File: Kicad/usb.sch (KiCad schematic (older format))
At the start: 1 part

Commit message: Completed Audio sheet.
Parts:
- gave numbers to parts that had none: 1
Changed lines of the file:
@@
 Sheet 5 9
 Title ""
-Date ""
+Date "2020-12-20"
 Rev ""
-Comp ""
-Comment1 ""
-Comment2 ""
+Comp "https://neotron-compute.github.io/"
+Comment1 "Licenced as CC BY-SA"
+Comment2 "Copyright (c) The Neotron Developers, 2020"
 Comment3 ""
 Comment4 ""
@@
 P 1700 1800
 AR Path="/5FDEB111" Ref="J?"  Part="1"
-AR Path="/5FDE7004/5FDEB111" Ref="J?"  Part="1"
-F 0 "J?" H 1757 2267 50  0000 C CNN
+AR Path="/5FDE7004/5FDEB111" Ref="J501"  Part="1"
+F 0 "J501" H 1757 2267 50  0000 C CNN
 F 1 "USB_A" H 1757 2176 50  0000 C CNN
 F 2 "Connector_USB:USB_A_Stewart_SS-52100-001_Horizontal" H 1850 1750 50  0001 C CNN

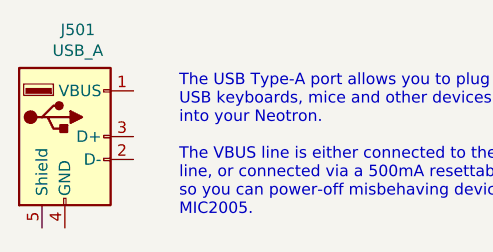
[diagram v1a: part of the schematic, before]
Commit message: Brought in RS232 circuit from Neotron 32.
Also updated 3D models.
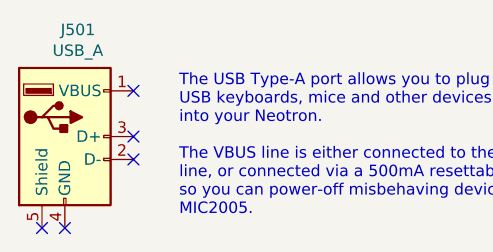
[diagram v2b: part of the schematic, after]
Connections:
- no-connect marks 0 -> 5
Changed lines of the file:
@@
 Text Notes 2200 2150 0    50   ~ 0
 The USB Type-A port allows you to plug\nUSB keyboards, mice and other devices\ninto your Neotron.\n\nThe VBUS line is either connected to the main 5V\nline, or connected via a 500mA resettable fuse/switch\nso you can power-off misbehaving devices. See\nMIC2005.
+NoConn ~ 2000 1600
+NoConn ~ 2000 1800
+NoConn ~ 2000 1900
+NoConn ~ 1600 2200
+NoConn ~ 1700 2200
 $EndSCHEMATC

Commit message: Updating BOM with parts.
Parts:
- J501: DNP (none) -> 0
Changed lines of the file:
@@
 F 2 "Connector_USB:USB_A_Stewart_SS-52100-001_Horizontal" H 1850 1750 50  0001 C CNN
 F 3 " ~" H 1850 1750 50  0001 C CNN
+F 4 "0" H 1700 1800 50  0001 C CNN "DNP"
 	1    1700 1800
 	1    0    0    -1

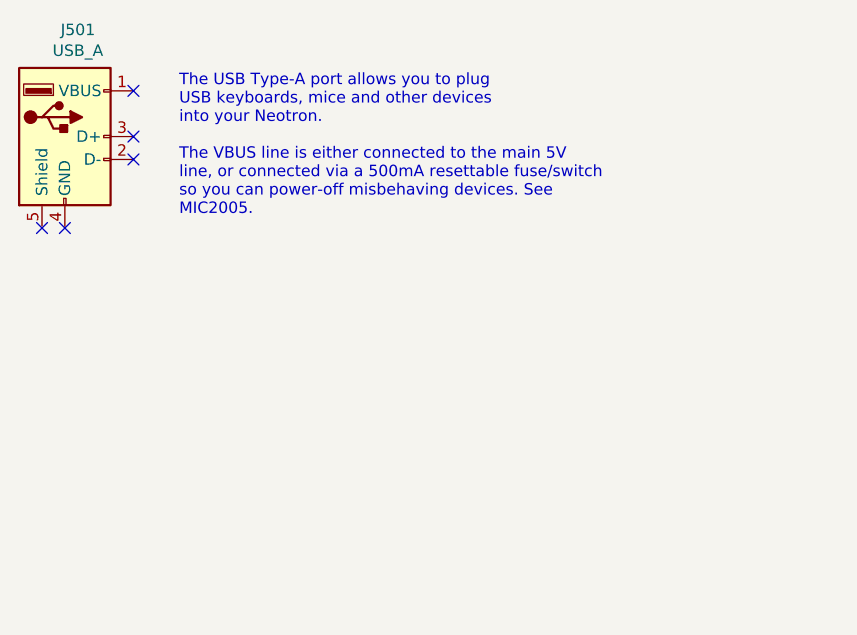
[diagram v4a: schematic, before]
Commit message: Added dual Type-A USB header.
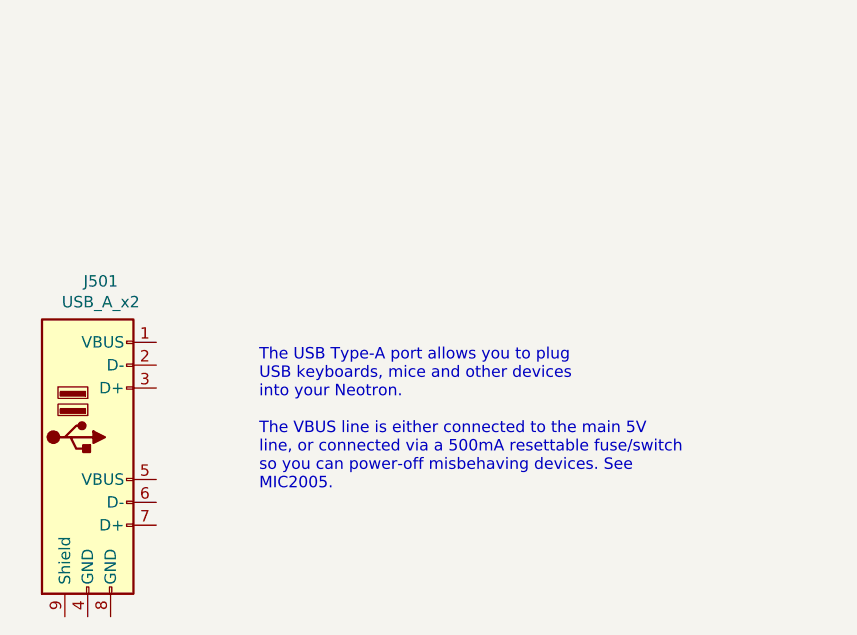
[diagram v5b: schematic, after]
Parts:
- removed J501: USB_A, Connector_USB:USB_A_Stewart_SS-52100-001_Horizontal, symbol Connector:USB_A
- added J501: USB_A_x2, Neotron-Common-Hardware:CUI_UJ2-ADH-1-TH, symbol Neotron-Common-Hardware:USB_A_x2
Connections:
- no-connect marks 5 -> 0
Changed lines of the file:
@@
 Comment4 ""
 $EndDescr
+Text Notes 2550 3350 0    50   ~ 0
+The USB Type-A port allows you to plug\nUSB keyboards, mice and other devices\ninto your Neotron.\n\nThe VBUS line is either connected to the main 5V\nline, or connected via a 500mA resettable fuse/switch\nso you can power-off misbehaving devices. See\nMIC2005.
 $Comp
-L Connector:USB_A J?
-U 1 1 5FDEB111
-P 1700 1800
-AR Path="/5FDEB111" Ref="J?"  Part="1"
-AR Path="/5FDE7004/5FDEB111" Ref="J501"  Part="1"
-F 0 "J501" H 1757 2267 50  0000 C CNN
-F 1 "USB_A" H 1757 2176 50  0000 C CNN
-F 2 "Connector_USB:USB_A_Stewart_SS-52100-001_Horizontal" H 1850 1750 50  0001 C CNN
-F 3 " ~" H 1850 1750 50  0001 C CNN
-F 4 "0" H 1700 1800 50  0001 C CNN "DNP"
-	1    1700 1800
+L Neotron-Common-Hardware:USB_A_x2 J501
+U 1 1 5FE385D9
+P 1800 3500
+F 0 "J501" H 1857 4567 50  0000 C CNN
+F 1 "USB_A_x2" H 1857 4476 50  0000 C CNN
+F 2 "Neotron-Common-Hardware:CUI_UJ2-ADH-1-TH" H 1750 4750 50  0001 C CNN
+F 3 "https://www.cuidevices.com/product/resource/digikeypdf/uj2-adh-th.pdf" H 1950 3550 50  0001 C CNN
+F 4 "CUI" H 1800 3500 50  0001 C CNN "Manufacturer"
+F 5 "UJ2-ADH-1-TH" H 1800 4650 50  0001 C CNN "MPN"
+F 6 "102-4001-ND" H 1800 4550 50  0001 C CNN "Digikey"
+	1    1800 3500
 	1    0    0    -1
 $EndComp
-Text Notes 2200 2150 0    50   ~ 0
-The USB Type-A port allows you to plug\nUSB keyboards, mice and other devices\ninto your Neotron.\n\nThe VBUS line is either connected to the main 5V\nline, or connected via a 500mA resettable fuse/switch\nso you can power-off misbehaving devices. See\nMIC2005.
-NoConn ~ 2000 1600
-NoConn ~ 2000 1800
-NoConn ~ 2000 1900
-NoConn ~ 1600 2200
-NoConn ~ 1700 2200
 $EndSCHEMATC

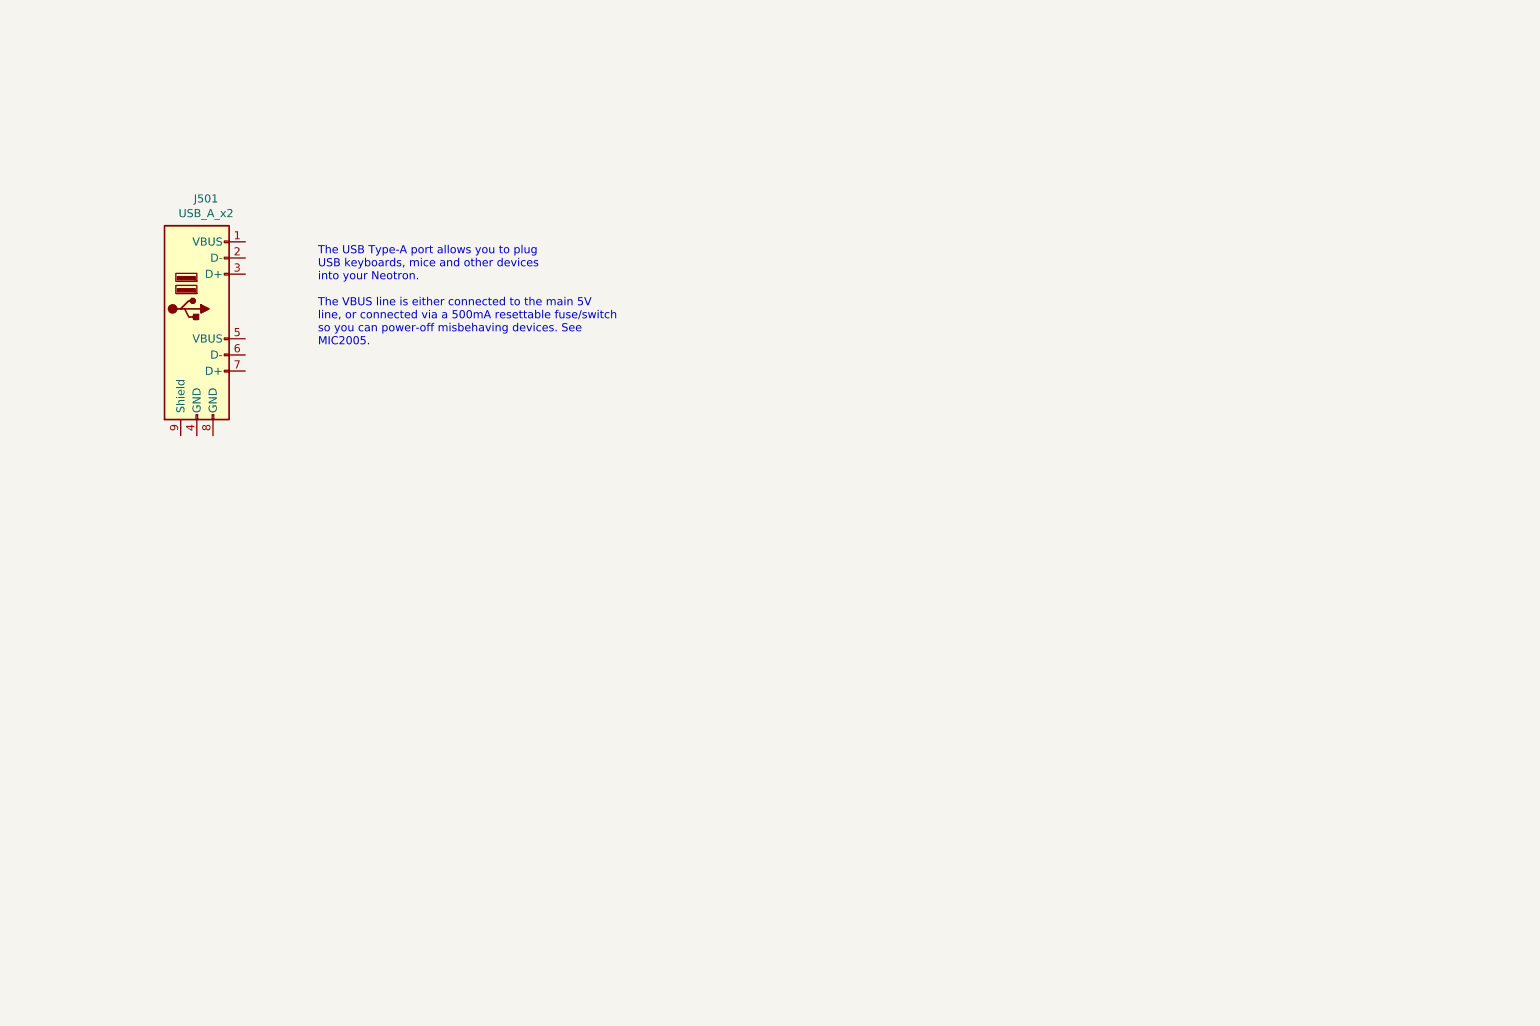
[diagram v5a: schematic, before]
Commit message: Working on VGA sheet and USB sheet.
Also added courtyard and silk to stacked USB connector.
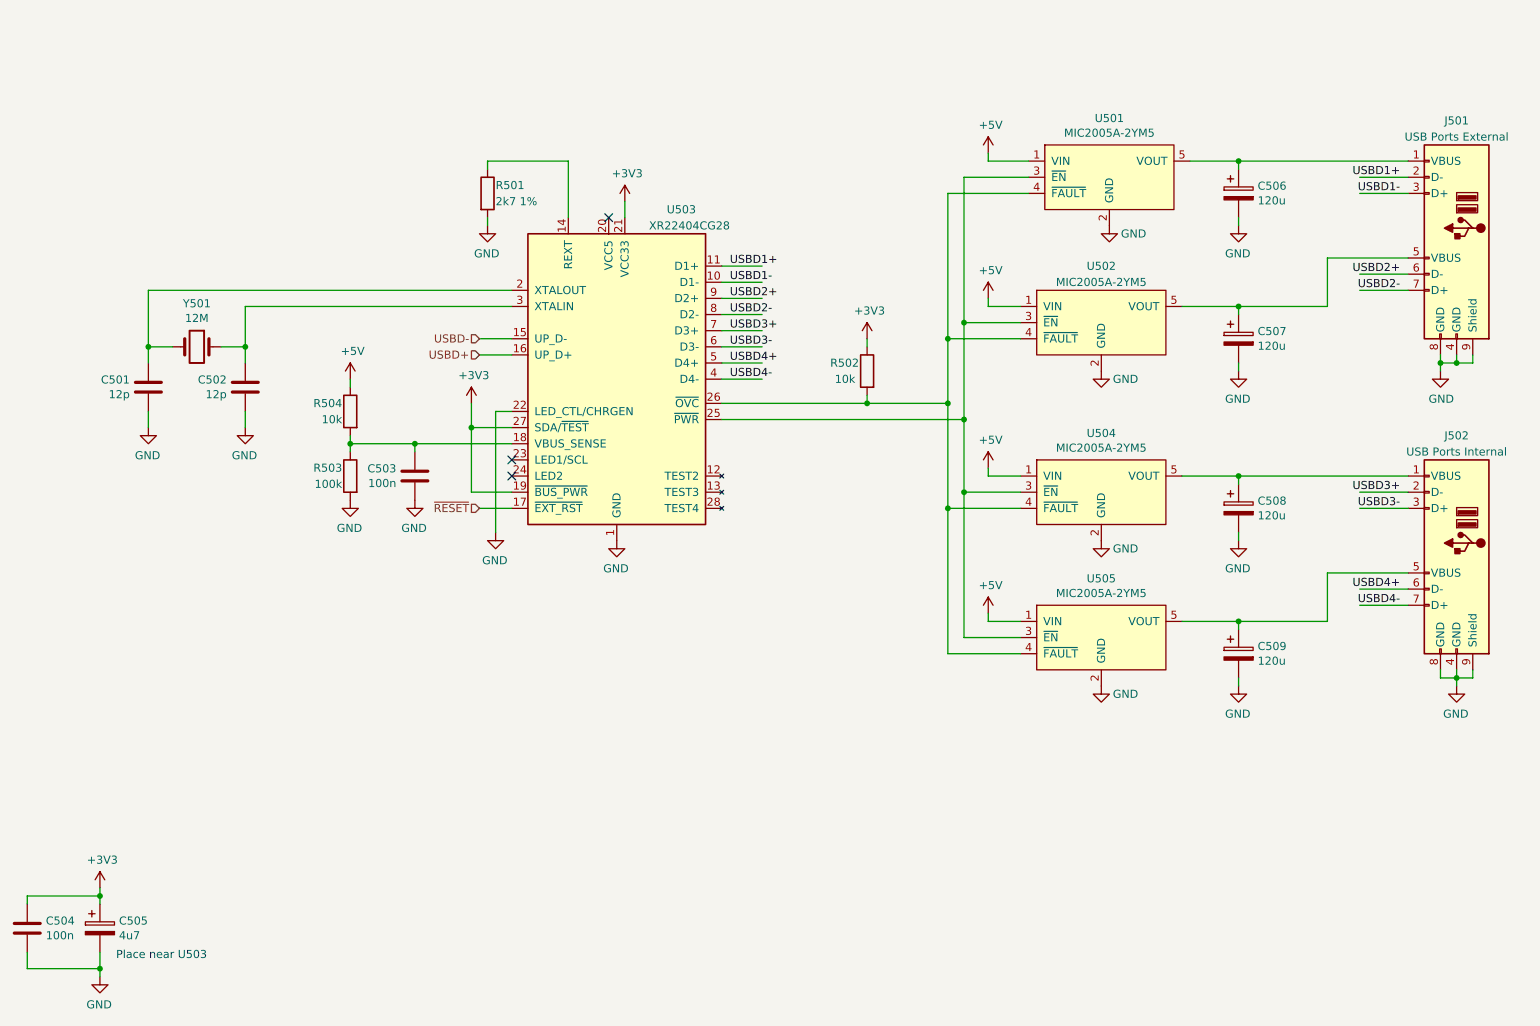
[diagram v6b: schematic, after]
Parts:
- added C501, C502: 12p, Capacitor_SMD:C_0805_2012Metric_Pad1.15x1.40mm_HandSolder, symbol Device:C
- added C503, C504: 100n, Capacitor_SMD:C_0805_2012Metric_Pad1.15x1.40mm_HandSolder, symbol Device:C
- added C505: 4u7, Capacitor_THT:CP_Radial_D6.3mm_P2.50mm, symbol Device:CP
- added C506, C507, C508, C509: 120u, Capacitor_THT:CP_Radial_D6.3mm_P2.50mm, symbol Device:CP
- added J502: USB Ports Internal, Neotron-Common-Hardware:USB_Header, symbol Neotron-Common-Hardware:USB_A_x2
- added R501: 2k7 1%, Resistor_SMD:R_0805_2012Metric_Pad1.15x1.40mm_HandSolder, symbol Device:R
- added R502, R504: 10k, Resistor_SMD:R_0805_2012Metric_Pad1.15x1.40mm_HandSolder, symbol Device:R
- added R503: 100k, Resistor_SMD:R_0805_2012Metric_Pad1.15x1.40mm_HandSolder, symbol Device:R
- added U501, U502, U504, U505: MIC2005A-2YM5, Package_TO_SOT_SMD:SOT-23-5_HandSoldering, symbol Neotron-Common-Hardware:MIC2005A-2YM5
- added U503: XR22404CG28, Package_SO:SSOP-28_3.9x9.9mm_P0.635mm, symbol Neotron-Common-Hardware:XR22404CG28
- added Y501: 12M, Crystal:Crystal_HC49-4H_Vertical, symbol Device:Crystal
- J501: value USB_A_x2 -> USB Ports External
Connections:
- net labels added: +3V3, +5V, GND, USBD+, USBD-, USBD1+, USBD1-, USBD2+, USBD2-, USBD3+, USBD3-, USBD4+, USBD4-, ~RESET
- wire segments 0 -> 115
- no-connect marks 0 -> 3
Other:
- note added: "Place near U503"
- note removed: "The USB Type-A port allows you to plug\nUSB keyboards, mice and other devices\ninto your Neotron.\n\nThe VBUS line is either connected to the main 5V\nline, or connected via a 500mA resettable fuse/switch\nso you can power-off misbehaving devices. See\nMIC2005."
- moved on the sheet: J501
